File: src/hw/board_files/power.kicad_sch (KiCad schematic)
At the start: 38 parts, among them P1 USB_C_Plug_USB2.0, SW1 SW_PWR, U1 TPS63031DSKR, U2 FT234XD-R, U3 MCP73831T-2ACI/OT

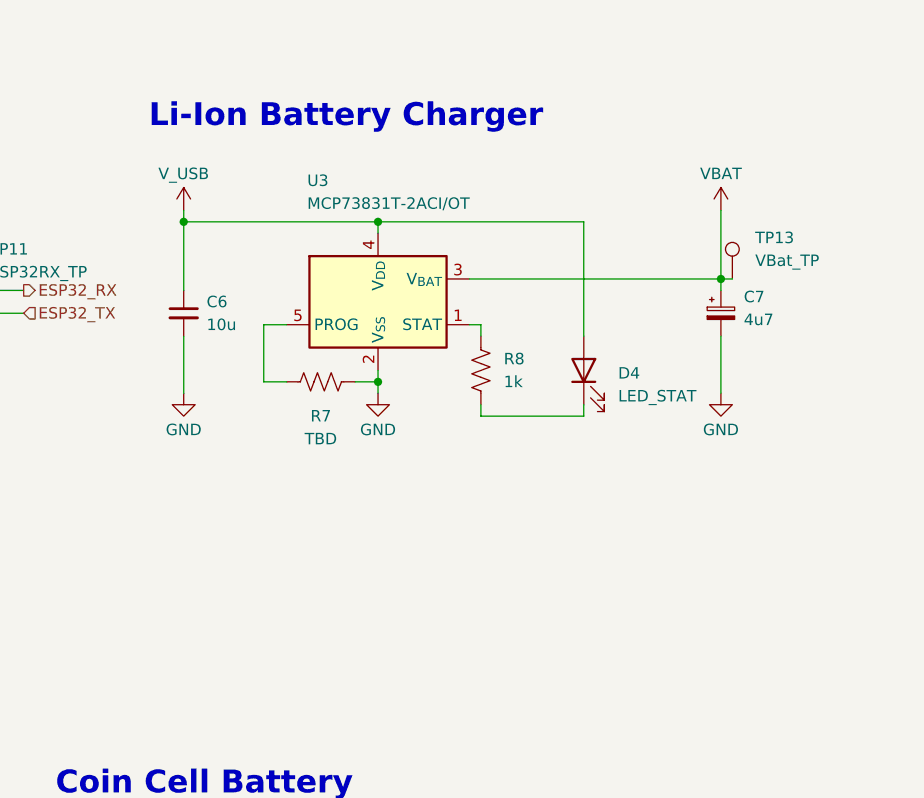
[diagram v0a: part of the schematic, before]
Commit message: Swapped LiPo charging IC to a smarter one prevents the system from drawing battery power when USB is plugged in
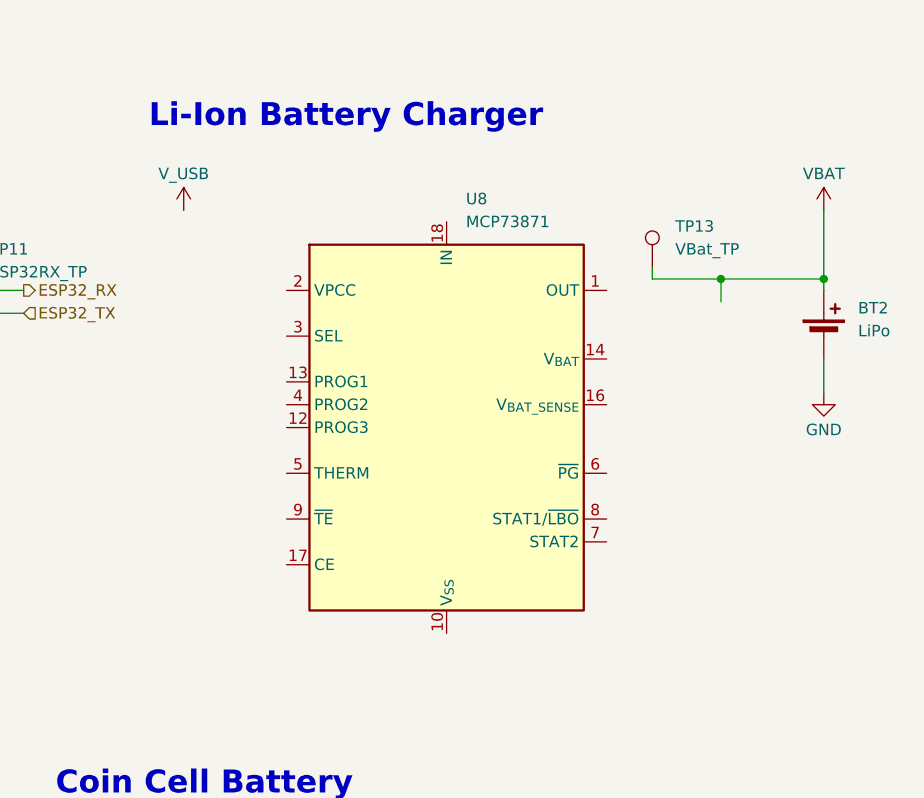
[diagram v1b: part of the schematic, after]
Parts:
- removed C6: 10u, Capacitor_SMD:C_0603_1608Metric, symbol Device:C_Small
- removed C7: 4u7, symbol Device:C_Polarized_Small
- removed D4: LED_STAT, LED_SMD:LED_0603_1608Metric, symbol Device:LED
- removed R7: TBD, Resistor_SMD:R_0603_1608Metric, symbol Device:R_US
- removed R8: 1k, Resistor_SMD:R_0603_1608Metric, symbol Device:R_US
- removed U3: MCP73831T-2ACI/OT, Package_TO_SOT_SMD:SOT-23-5, symbol Battery_Management:MCP73831-2-OT
- added BT2: LiPo, Connector_JST:JST_PH_S2B-PH-K_1x02_P2.00mm_Horizontal, symbol Device:Battery_Cell
- added U8: MCP73871, Package_DFN_QFN:QFN-20-1EP_4x4mm_P0.5mm_EP2.5x2.5mm, symbol Battery_Management:MCP73871
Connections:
- net GND: now also BT2.2 (-)
- net VBAT: now also BT2.1 (+)
- new net: U8.1 (OUT), U8.20 (OUT)
- new net: U8.10 (V_{SS}), U8.11 (V_{SS}), U8.21 (V_{SS})
- new net: U8.14 (V_{BAT}), U8.15 (V_{BAT})
- new net: U8.18 (IN), U8.19 (IN)
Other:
- moved on the sheet: TP13

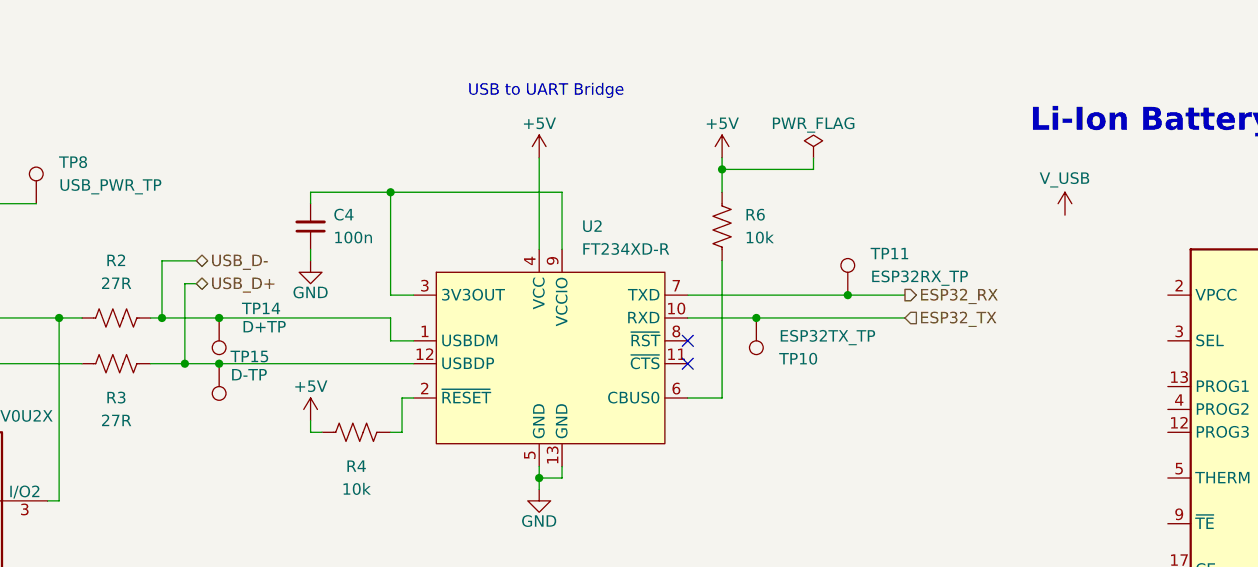
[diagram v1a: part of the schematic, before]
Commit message: Changed some jumpers to 3 pin headers
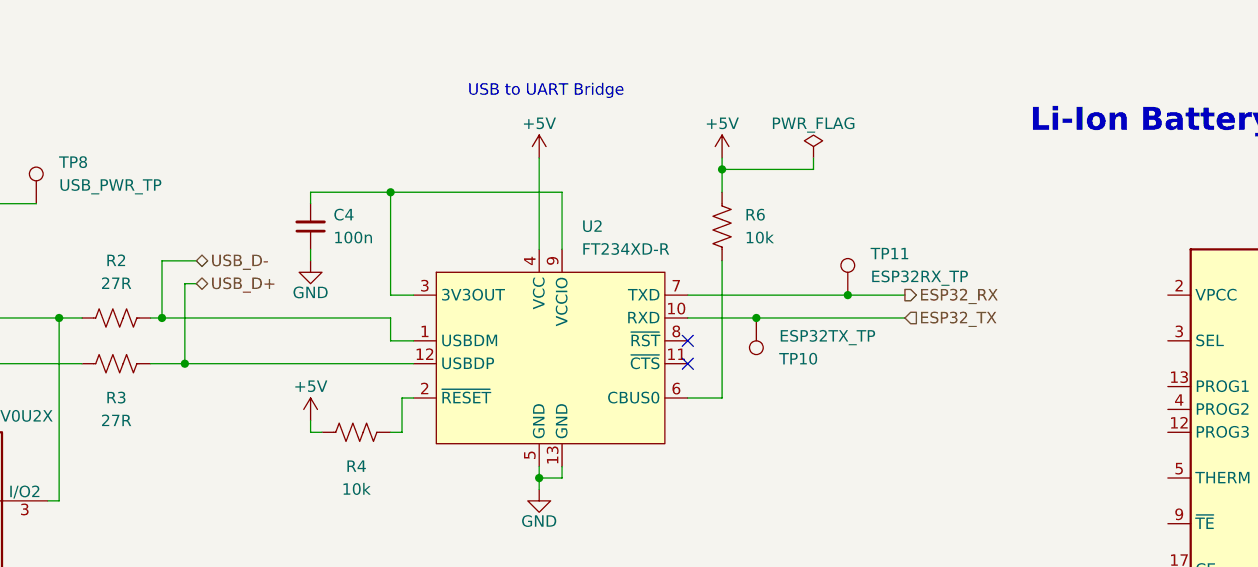
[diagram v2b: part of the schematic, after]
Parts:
- removed TP14: D+TP, symbol Connector:TestPoint
- removed TP15: D-TP, symbol Connector:TestPoint
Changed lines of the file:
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@@
 	)
 	(junction
-		(at 113.03 62.23)
-		(diameter 0)
-		(color 0 0 0 0)
-	)
-	(junction
 		(at 182.88 59.69)
 		(diameter 0)
@@
 	)
 	(junction
-		(at 113.03 67.31)
-		(diameter 0)
-		(color 0 0 0 0)
-	)
-	(junction
 		(at 109.22 67.31)
 		(diameter 0)
@@
 	(wire
 		(pts
-			(xy 113.03 67.31) (xy 134.62 67.31)
-		)
-		(stroke
-			(width 0)
-			(type default)
-		)
-	)
-	(wire
-		(pts
 			(xy 148.59 78.74) (xy 148.59 80.01)
 		)
@@
 	(wire
 		(pts
-			(xy 113.03 62.23) (xy 132.08 62.23)
-		)
-		(stroke
-			(width 0)
-			(type default)
-		)
-	)
-	(wire
-		(pts
 			(xy 39.37 138.43) (xy 39.37 143.51)
 		)
@@
 	(wire
 		(pts
-			(xy 106.68 62.23) (xy 113.03 62.23)
+			(xy 106.68 62.23) (xy 132.08 62.23)
 		)
 		(stroke
@@
 	(wire
 		(pts
-			(xy 109.22 67.31) (xy 113.03 67.31)
+			(xy 109.22 67.31) (xy 134.62 67.31)
 		)
 		(stroke
@@
 	)
 	(symbol
-		(lib_id "power:+5V")
-		(at 207.01 50.8 0)
-		(unit 1)
-		(exclude_from_sim no)
-		(in_bom yes)
-		(on_board yes)
-		(dnp no)
-		(property "Reference" "#PWR024"
-			(at 207.01 54.61 0)
-			(effects
-				(font
-					(size 1.27 1.27)
-				)
-				(hide yes)
-			)
-		)
-		(property "Value" "V_USB"
-			(at 207.01 46.736 0)
-			(effects
-				(font
-					(size 1.27 1.27)
-				)
-			)
-		)
-		(property "Footprint" ""
-			(at 207.01 50.8 0)
-			(effects
-				(font
-					(size 1.27 1.27)
-				)
-				(hide yes)
-			)
-		)
-		(property "Datasheet" ""
-			(at 207.01 50.8 0)
-			(effects
-				(font
-					(size 1.27 1.27)
-				)
-				(hide yes)
-			)
-		)
-		(property "Description" "Power symbol creates a global label with name \"+5V\""
-			(at 207.01 50.8 0)
-			(effects
-				(font
-					(size 1.27 1.27)
-				)
-				(hide yes)
-			)
-		)
-		(pin "1"
-		)
-		(instances
-			(project "pocket-caddy"
-				(path "/2c77a8ba-b277-4959-adec-d3fc778c7960/7763c5b3-a08f-479a-9f6f-ea394e6f7159"
-					(reference "#PWR024")
-					(unit 1)
-				)
-			)
-		)
-	)
-	(symbol
 		(lib_id "Connector:TestPoint")
 		(at 259.08 57.15 0)
@@
 	)
 	(symbol
-		(lib_id "Connector:TestPoint")
-		(at 113.03 62.23 180)
-		(unit 1)
-		(exclude_from_sim no)
-		(in_bom yes)
-		(on_board yes)
-		(dnp no)
-		(property "Reference" "TP14"
-			(at 115.57 61.214 0)
-			(effects
-				(font
-					(size 1.27 1.27)
-				)
-				(justify right)
-			)
-		)
-		(property "Value" "D+TP"
-			(at 115.57 63.246 0)
-			(effects
-				(font
-					(size 1.27 1.27)
-				)
-				(justify right)
-			)
-		)
-		(property "Footprint" ""
-			(at 107.95 62.23 0)
-			(effects
-				(font
-					(size 1.27 1.27)
-				)
-				(hide yes)
-			)
-		)
-		(property "Datasheet" "~"
-			(at 107.95 62.23 0)
-			(effects
-				(font
-					(size 1.27 1.27)
-				)
-				(hide yes)
-			)
-		)
-		(property "Description" "test point"
-			(at 113.03 62.23 0)
-			(effects
-				(font
-					(size 1.27 1.27)
-				)
-				(hide yes)
-			)
-		)
-		(pin "1"
-		)
-		(instances
-			(project ""
-				(path "/2c77a8ba-b277-4959-adec-d3fc778c7960/7763c5b3-a08f-479a-9f6f-ea394e6f7159"
-					(reference "TP14")
-					(unit 1)
-				)
-			)
-		)
-	)
-	(symbol
 		(lib_id "Device:R_US")
 		(at 55.88 78.74 180)
@@
 					(unit 1)
 				)
-			)
-		)
-	)
-	(symbol
-		(lib_id "Connector:TestPoint")
-		(at 113.03 67.31 180)
-		(unit 1)
-		(exclude_from_sim no)
-		(in_bom yes)
-		(on_board yes)
-		(dnp no)
-		(property "Reference" "TP15"
-			(at 114.3 66.548 0)
-			(effects
-				(font
-					(size 1.27 1.27)
-				)
-				(justify right)
-			)
-		)
-		(property "Value" "D-TP"
-			(at 114.3 68.58 0)
-			(effects
-				(font
-					(size 1.27 1.27)
-				)
-				(justify right)
-			)
-		)
-		(property "Footprint" ""
-			(at 107.95 67.31 0)
-			(effects
-				(font
-					(size 1.27 1.27)
-				)
-				(hide yes)
-			)
-		)
-		(property "Datasheet" "~"
-			(at 107.95 67.31 0)
-			(effects
-				(font
-					(size 1.27 1.27)
-				)
-				(hide yes)
-			)
-		)
-		(property "Description" "test point"
-			(at 113.03 67.31 0)
-			(effects
-				(font
-					(size 1.27 1.27)
-				)
-				(hide yes)
-			)
-		)
-		(pin "1"
-		)
-		(instances
-			(project ""
-				(path "/2c77a8ba-b277-4959-adec-d3fc778c7960/7763c5b3-a08f-479a-9f6f-ea394e6f7159"
-					(reference "TP15")
-					(unit 1)
-				)

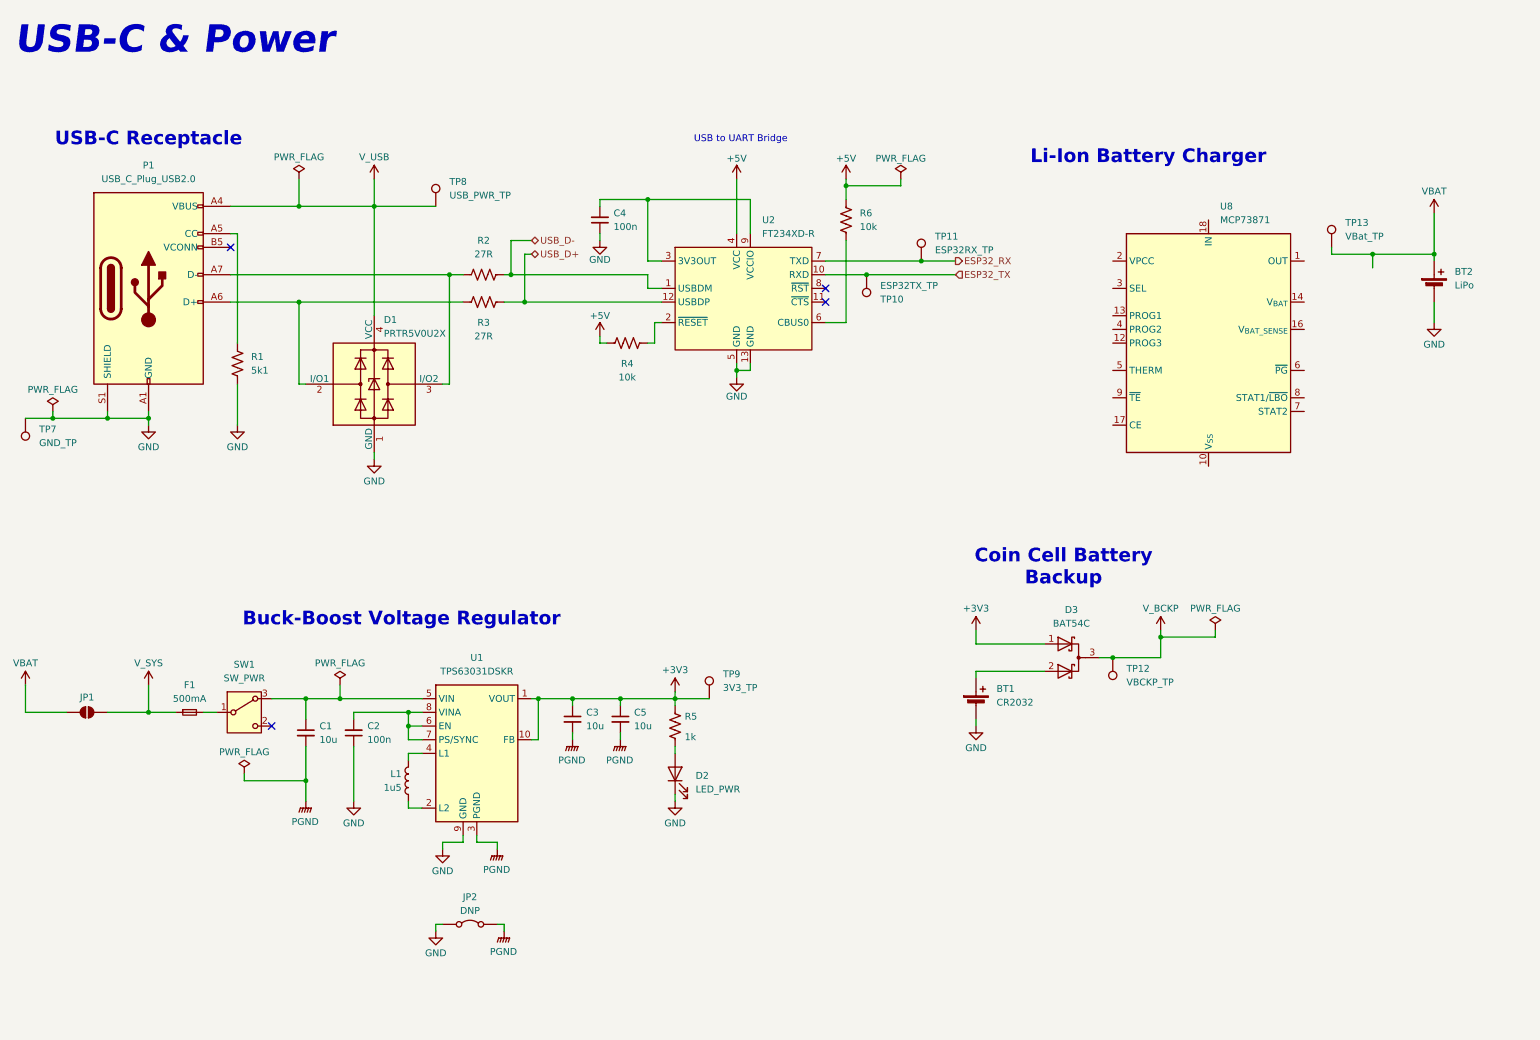
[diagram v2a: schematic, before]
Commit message: Added parts for new IC
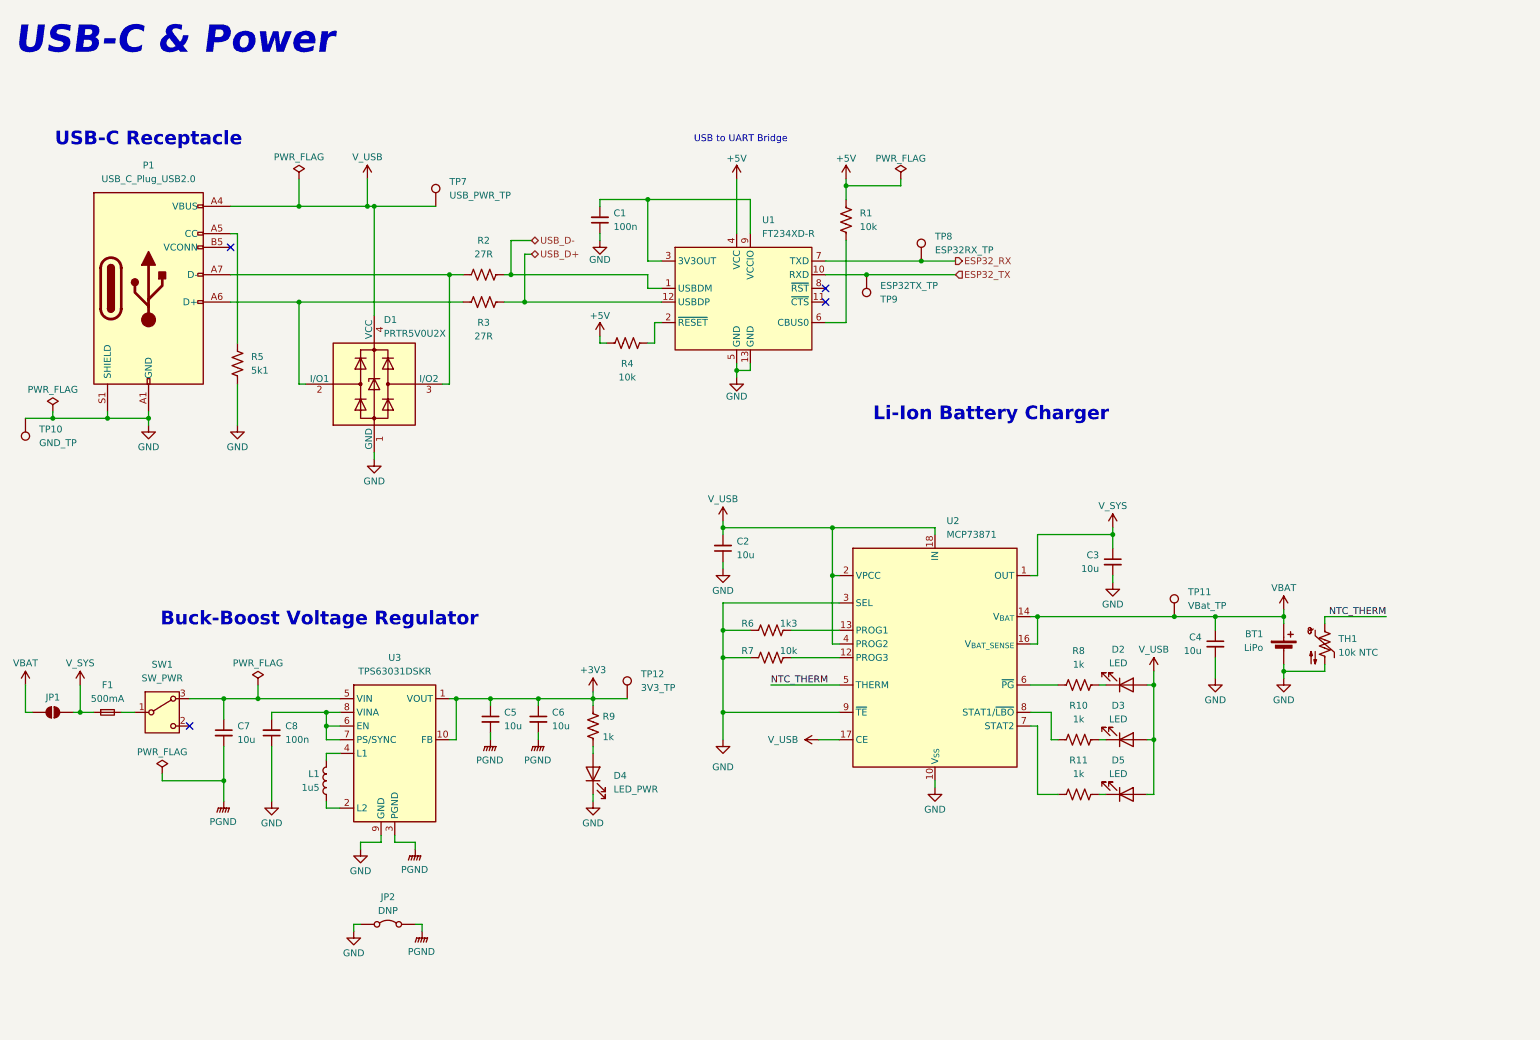
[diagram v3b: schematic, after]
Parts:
- removed BT1: CR2032, Battery:BatteryHolder_Keystone_3002_1x2032, symbol Device:Battery_Cell
- removed D3: BAT54C, Package_TO_SOT_SMD:SOT-23-3, symbol Device:D_Schottky_Dual_CommonCathode_AAK_Parallel
- removed TP12: VBCKP_TP, symbol Connector:TestPoint
- added C2, C3, C4: 10u, Capacitor_SMD:C_0504_1310Metric_Pad0.83x1.28mm_HandSolder, symbol Device:C_Small
- added D2, D3, D5: LED, LED_SMD:LED_0603_1608Metric_Pad1.05x0.95mm_HandSolder, symbol Device:LED
- added R10, R11, R8: 1k, Resistor_SMD:R_0603_1608Metric_Pad0.98x0.95mm_HandSolder, symbol Device:R_US
- added R6: 1k3, Resistor_SMD:R_0603_1608Metric_Pad0.98x0.95mm_HandSolder, symbol Device:R_US
- added R7: 10k, Resistor_SMD:R_0603_1608Metric_Pad0.98x0.95mm_HandSolder, symbol Device:R_US
- added TH1: 10k NTC, symbol Device:Thermistor_NTC_US
- C1: renamed from C4; footprint Capacitor_SMD:C_0603_1608Metric -> Capacitor_SMD:C_0504_1310Metric_Pad0.83x1.28mm_HandSolder
- C5: renamed from C3; footprint Capacitor_SMD:C_0603_1608Metric -> Capacitor_SMD:C_0504_1310Metric_Pad0.83x1.28mm_HandSolder
- C6: renamed from C5; footprint Capacitor_SMD:C_0603_1608Metric -> Capacitor_SMD:C_0504_1310Metric_Pad0.83x1.28mm_HandSolder
- C7: renamed from C1; footprint Capacitor_SMD:C_0603_1608Metric -> Capacitor_SMD:C_0504_1310Metric_Pad0.83x1.28mm_HandSolder
- C8: renamed from C2; footprint Capacitor_SMD:C_0603_1608Metric -> Capacitor_SMD:C_0504_1310Metric_Pad0.83x1.28mm_HandSolder
- D4: renamed from D2; footprint LED_SMD:LED_0603_1608Metric -> LED_SMD:LED_0603_1608Metric_Pad1.05x0.95mm_HandSolder
- R1: renamed from R6; footprint Resistor_SMD:R_0603_1608Metric -> Resistor_SMD:R_0603_1608Metric_Pad0.98x0.95mm_HandSolder
- R2, R3, R4: footprint Resistor_SMD:R_0603_1608Metric -> Resistor_SMD:R_0603_1608Metric_Pad0.98x0.95mm_HandSolder
- R5: renamed from R1; footprint Resistor_SMD:R_0603_1608Metric -> Resistor_SMD:R_0603_1608Metric_Pad0.98x0.95mm_HandSolder
- R9: renamed from R5; footprint Resistor_SMD:R_0603_1608Metric -> Resistor_SMD:R_0603_1608Metric_Pad0.98x0.95mm_HandSolder
- renumbered BT2 to BT1, TP7 to TP10, TP13 to TP11, TP9 to TP12, TP8 to TP7, TP11 to TP8, TP10 to TP9, U2 to U1, U8 to U2, U1 to U3
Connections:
- net GND: now also U2.10 (V_{SS}), U2.11 (V_{SS}), U2.21 (V_{SS}), U2.3 (SEL), U2.9 (~{TE}), C2.1, C3.2, C4.2, R6.1, R7.1, TH1.2
- net VBAT: now also U2.14 (V_{BAT}), U2.15 (V_{BAT}), U2.16 (V_{BAT_SENSE}), C4.1
- net V_SYS: now also U2.1 (OUT), U2.20 (OUT), C3.1
- net V_USB: now also U2.17 (CE), U2.18 (IN), U2.19 (IN), U2.2 (VPCC), U2.4 (PROG2), C2.2, D2.2 (A), D3.2 (A), D5.2 (A)
- net at U2.12 (PROG3): now also R7.2
- net at U2.13 (PROG1): now also R6.2
- net NTC_THERM: now reaches U2.5 (THERM)
- net NTC_THERM: now also TH1.1
- net at U2.6 (~{PG}): now also R8.1
- net at U2.7 (STAT2): now also R11.1
- net at U2.8 (STAT1/~{LBO}): now also R10.1
- new net: D2.1 (K), R8.2
- new net: D3.1 (K), R10.2
- new net: D5.1 (K), R11.2
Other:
- note removed: "Coin Cell Battery Backup"
- moved on the sheet: BT1, C5, C6, C7, C8, D4, F1, JP1, JP2, L1, R9, SW1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
